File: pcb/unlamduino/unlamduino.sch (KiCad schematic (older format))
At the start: 46 parts, among them IC2 ATMEGA328-P, P3 CONN_01X08, U1 LM2576, U2 AP111733, Y2 16MHz

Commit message: cambio huella de regulador de 3v3. Marca Tx y Rx cerca conector.
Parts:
- JP1: footprint (none) -> Connect:BARREL_JACK
- U2: footprint TO_SOT_Packages_SMD:SOT-223 -> TO_SOT_Packages_SMD:TO-252-2Lead
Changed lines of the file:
@@
 F 0 "U2" H 7750 1650 50  0000 C CNN
 F 1 "AP111733" H 7650 2150 50  0000 C CNN
-F 2 "TO_SOT_Packages_SMD:SOT-223" H 7650 1550 50  0001 C CNN
+F 2 "TO_SOT_Packages_SMD:TO-252-2Lead" H 7650 1550 50  0001 C CNN
 F 3 "" H 7750 1650 50  0000 C CNN
 	1    7650 1900
@@
 F 0 "JP1" H 2200 1700 50  0000 C CNN
 F 1 "BARREL_JACK" H 2200 1250 50  0000 C CNN
-F 2 "" H 2200 1450 50  0000 C CNN
+F 2 "Connect:BARREL_JACK" H 2200 1450 50  0001 C CNN
 F 3 "" H 2200 1450 50  0000 C CNN
 	1    2200 1450

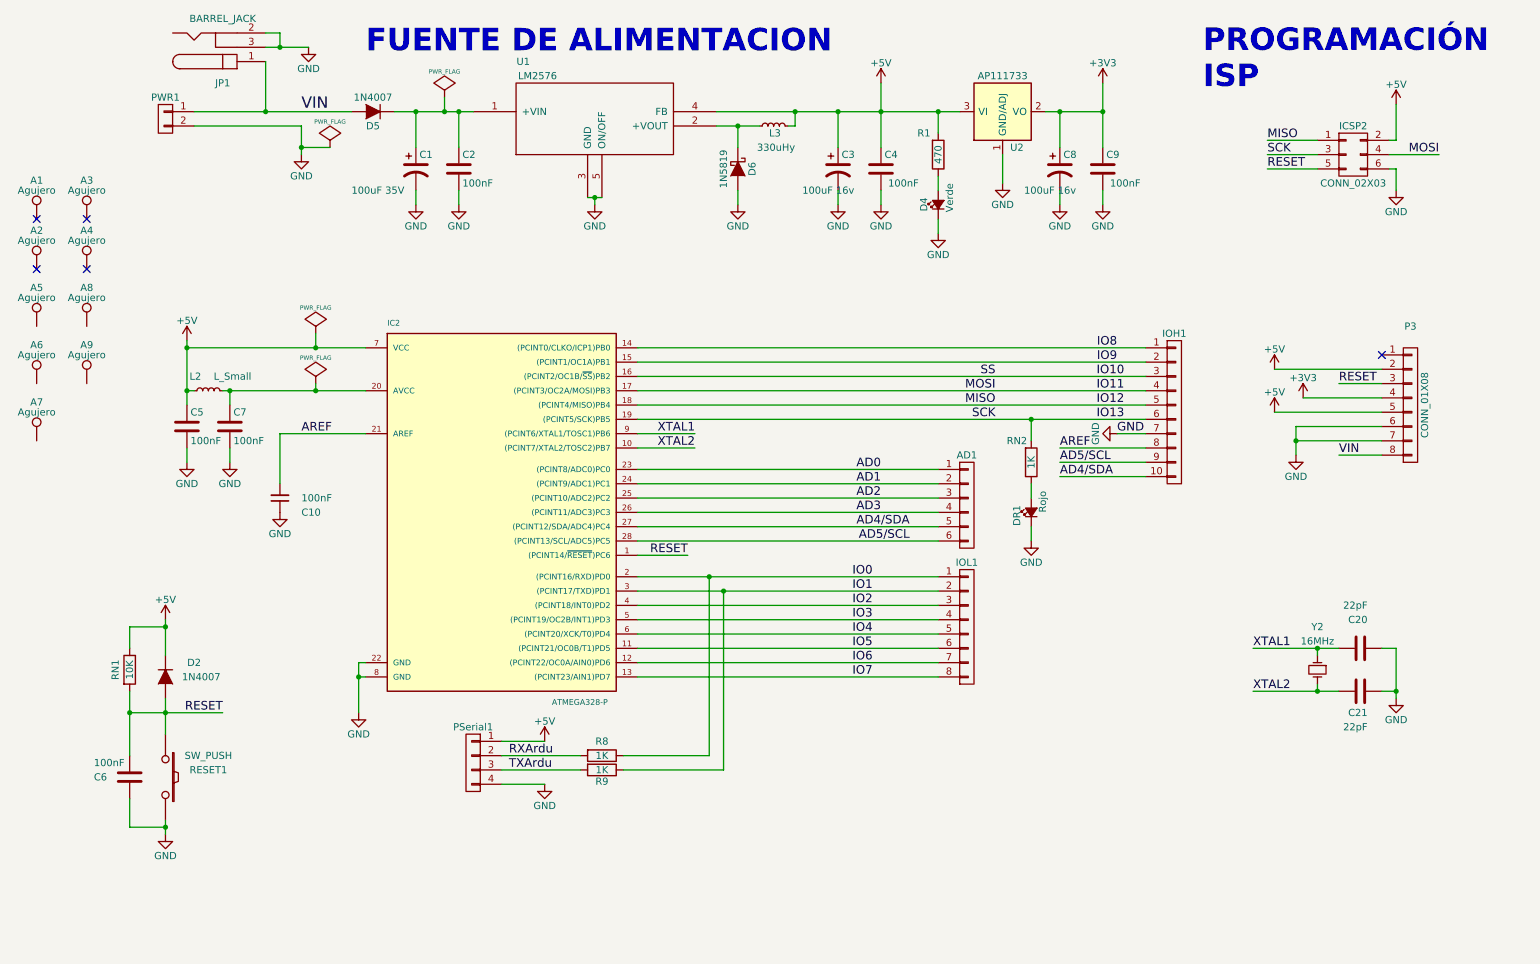
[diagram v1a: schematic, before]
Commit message: Agregado de la definición del cable serie para programar en niveles TTL.
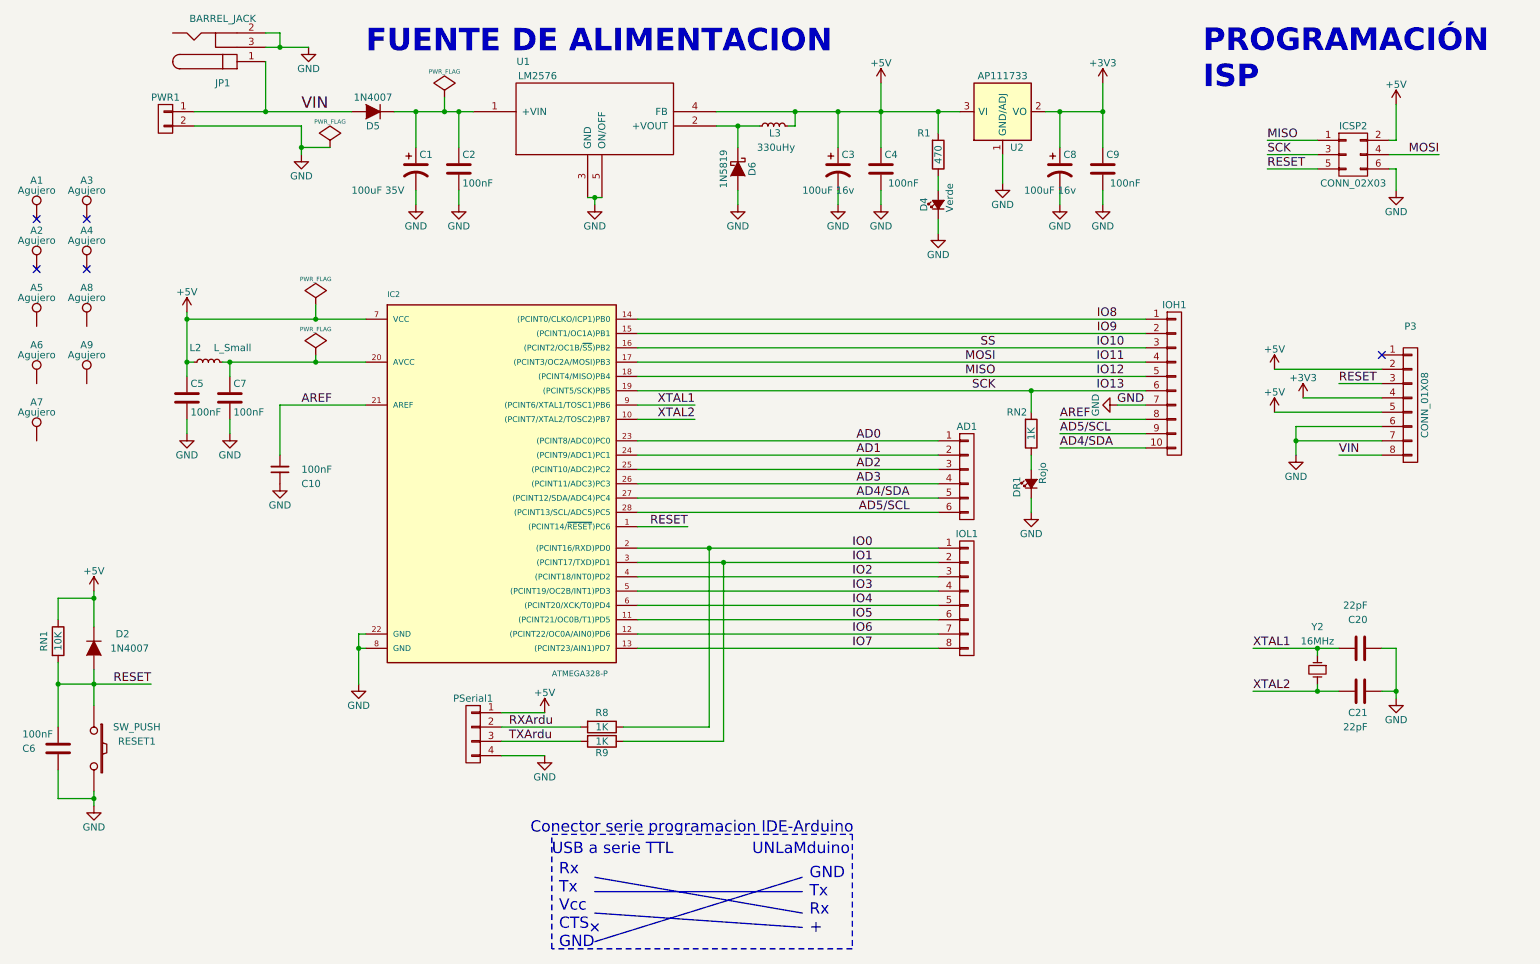
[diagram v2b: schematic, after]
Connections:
- no-connect marks 5 -> 6
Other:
- note added: "Conector serie programacion IDE-Arduino"
- note added: "GND\nTx\nRx\n+"
- note added: "Rx\nTx\nVcc\nCTS\nGND"
- note added: "UNLaMduino"
- note added: "USB a serie TTL"
- moved on the sheet: AD1, C10, C5, C6, C7, D2, DR1, IC2, IOH1, IOL1, L2, PSerial1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
